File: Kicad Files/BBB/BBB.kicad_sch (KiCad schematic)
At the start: 36 parts, among them J1 PPTC041LFBN-RC, J2 PPTC041LFBN-RC, J3 PPTC041LFBN-RC, J4 PPTC061LFBN-RC, J5 Jumper_NO, J6 PPTC041LFBN-RC, P1 3220-20-0200-00, U1 STM32WBA50KGU6, U2 LM393F-GE2, Y1 ABS07AIG-32.768KHZ-T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

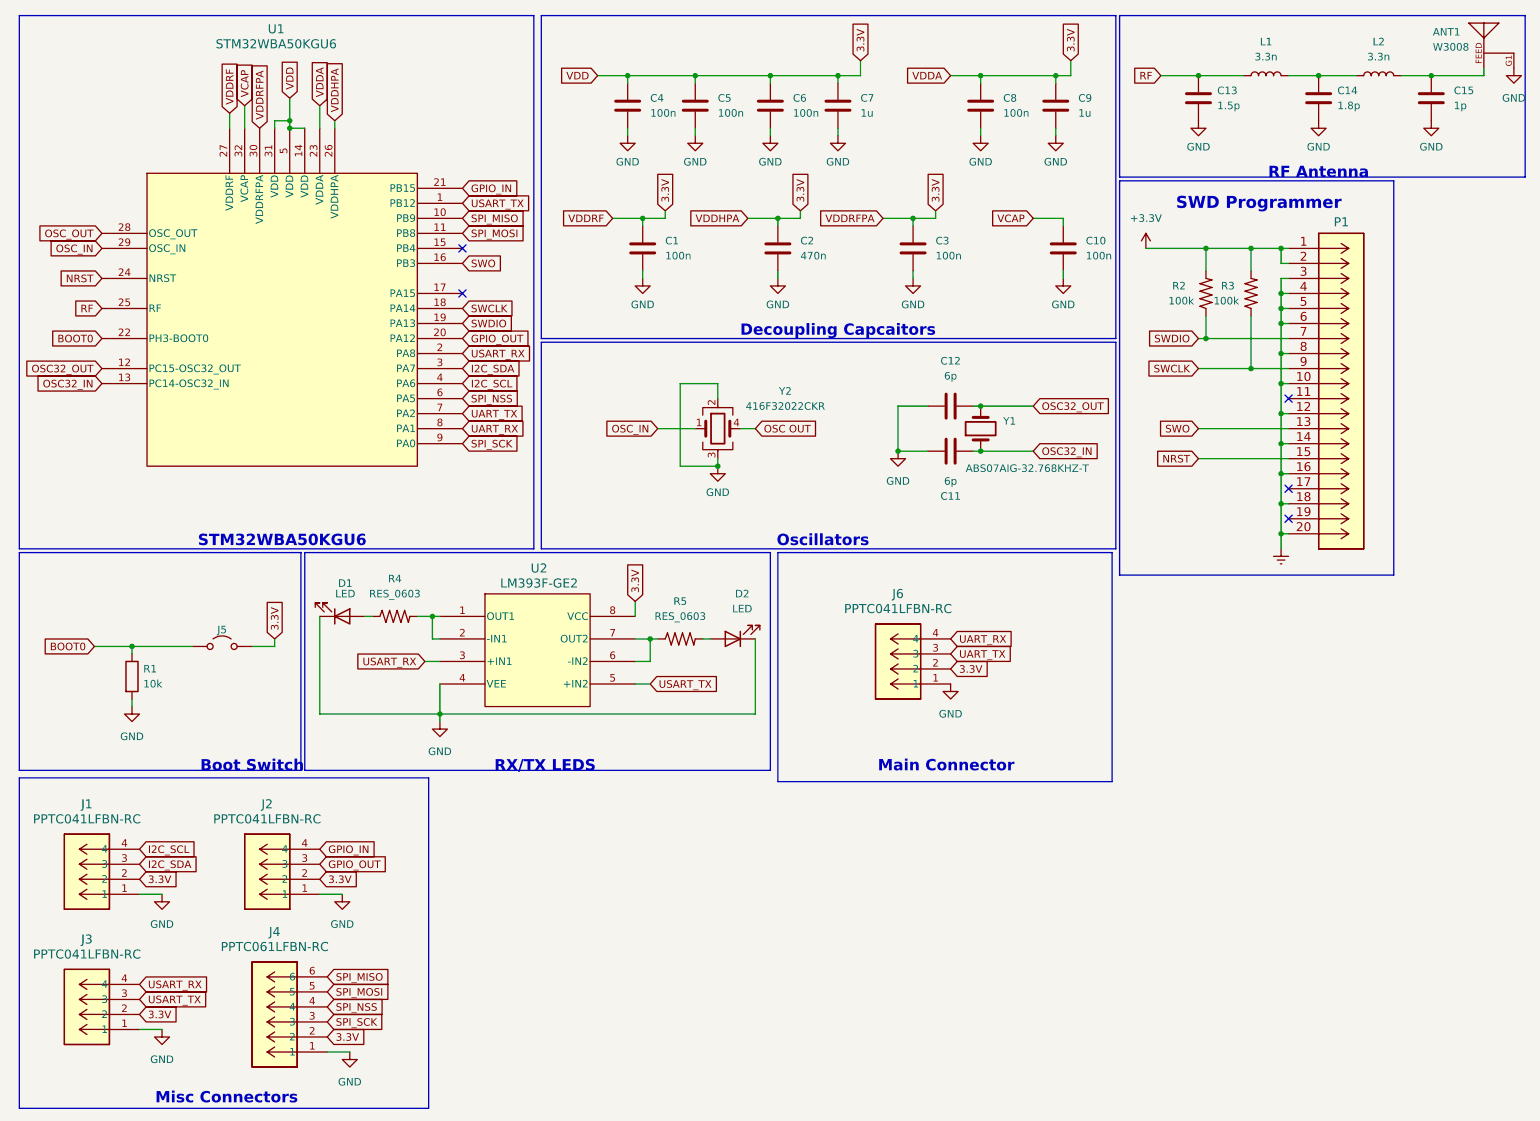
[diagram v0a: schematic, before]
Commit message: BBB Board
Designed basic breakout board for the STMWBA chip
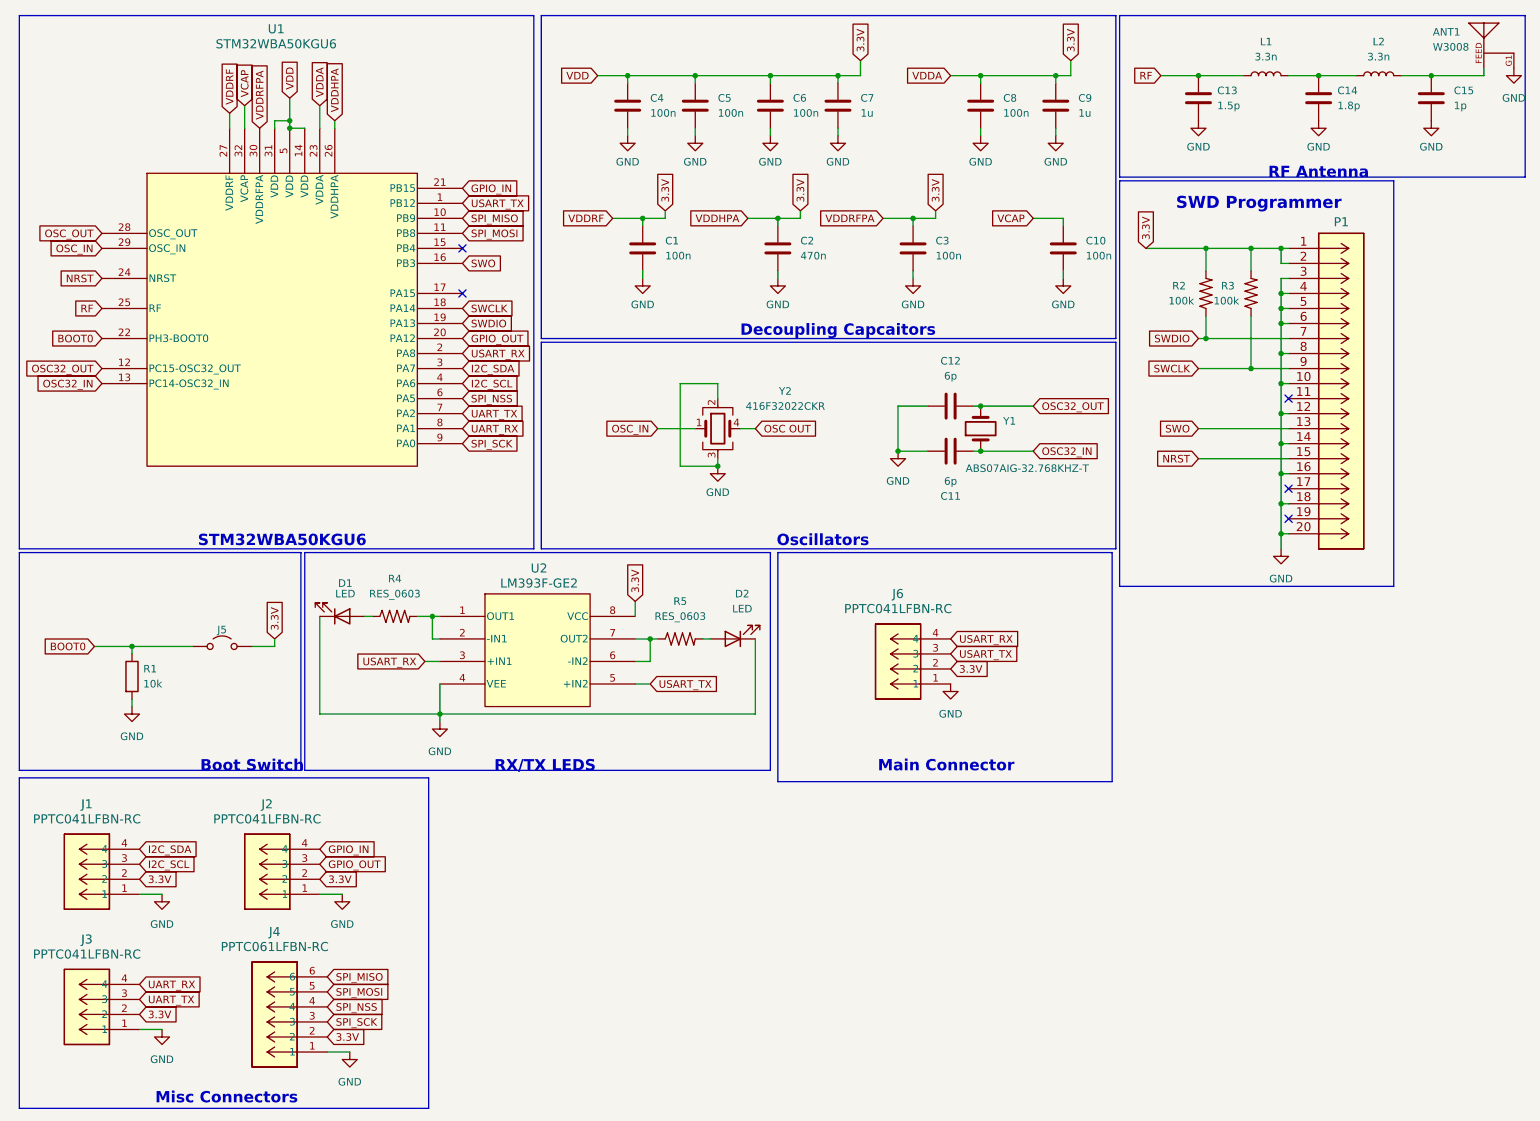
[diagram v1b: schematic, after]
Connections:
- net +3.3V is gone; now on net 3.3V: P1.1, P1.2, R2.2, R3.2
- net Earth is gone; now on net GND: P1.10, P1.12, P1.14, P1.16, P1.18, P1.20, P1.3, P1.4, P1.5, P1.6, P1.8
- net I2C_SCL: now also J1.3; no longer J1.4
- net I2C_SDA: now also J1.4; no longer J1.3
- net UART_RX: now also J3.4; no longer J6.4
- net UART_TX: now also J3.3; no longer J6.3
- net USART_RX: now also J6.4; no longer J3.4
- net USART_TX: now also J6.3; no longer J3.3
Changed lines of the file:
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@@
 	(rectangle
 		(start 198.755 40.64)
-		(end 245.11 107.315)
+		(end 245.11 109.22)
 		(stroke
 			(width 0)
@@
 		)
 	)
+	(global_label "3.3V"
+		(shape input)
+		(at 203.2 52.07 90)
+		(fields_autoplaced yes)
+		(effects
+			(font
+				(size 1.27 1.27)
+			)
+			(justify left)
+		)
+		(property "Intersheetrefs" "${INTERSHEET_REFS}"
+			(at 203.2 44.9724 90)
+			(effects
+				(font
+					(size 1.27 1.27)
+				)
+				(justify left)
+				(hide yes)
+			)
+		)
+	)
 	(global_label "RF"
 		(shape input)
@@
 		)
 	)
-	(global_label "I2C_SCL"
+	(global_label "I2C_SDA"
 		(shape input)
 		(at 33.02 153.67 0)
@@
 		)
 		(property "Intersheetrefs" "${INTERSHEET_REFS}"
-			(at 43.5647 153.67 0)
+			(at 43.6252 153.67 0)
 			(effects
 				(font
@@
 		)
 	)
-	(global_label "I2C_SDA"
+	(global_label "I2C_SCL"
 		(shape input)
 		(at 33.02 156.21 0)
@@
 		)
 		(property "Intersheetrefs" "${INTERSHEET_REFS}"
-			(at 43.6252 156.21 0)
+			(at 43.5647 156.21 0)
 			(effects
 				(font
@@
 		)
 	)
-	(global_label "UART_TX"
+	(global_label "USART_TX"
 		(shape input)
 		(at 170.18 120.65 0)
@@
 		)
 		(property "Intersheetrefs" "${INTERSHEET_REFS}"
-			(at 180.9666 120.65 0)
+			(at 182.1761 120.65 0)
 			(effects
 				(font
@@
 		)
 	)
-	(global_label "USART_TX"
+	(global_label "UART_TX"
 		(shape input)
 		(at 33.02 179.07 0)
@@
 		)
 		(property "Intersheetrefs" "${INTERSHEET_REFS}"
-			(at 45.0161 179.07 0)
+			(at 43.8066 179.07 0)
 			(effects
 				(font
@@
 		)
 	)
-	(global_label "USART_RX"
+	(global_label "UART_RX"
 		(shape input)
 		(at 33.02 176.53 0)
@@
 		)
 		(property "Intersheetrefs" "${INTERSHEET_REFS}"
-			(at 45.3185 176.53 0)
+			(at 44.109 176.53 0)
 			(effects
 				(font
@@
 		)
 	)
-	(global_label "UART_RX"
+	(global_label "USART_RX"
 		(shape input)
 		(at 170.18 118.11 0)
@@
 		)
 		(property "Intersheetrefs" "${INTERSHEET_REFS}"
-			(at 181.269 118.11 0)
+			(at 182.4785 118.11 0)
 			(effects
 				(font
@@
 	)
 	(symbol
+		(lib_id "power:GND")
+		(at 226.06 102.87 0)
+		(unit 1)
+		(exclude_from_sim no)
+		(in_bom yes)
+		(on_board yes)
+		(dnp no)
+		(fields_autoplaced yes)
+		(property "Reference" "#PWR01"
+			(at 226.06 109.22 0)
+			(effects
+				(font
+					(size 1.27 1.27)
+				)
+				(hide yes)
+			)
+		)
+		(property "Value" "GND"
+			(at 226.06 107.95 0)
+			(effects
+				(font
+					(size 1.27 1.27)
+				)
+			)
+		)
+		(property "Footprint" ""
+			(at 226.06 102.87 0)
+			(effects
+				(font
+					(size 1.27 1.27)
+				)
+				(hide yes)
+			)
+		)
+		(property "Datasheet" ""
+			(at 226.06 102.87 0)
+			(effects
+				(font
+					(size 1.27 1.27)
+				)
+				(hide yes)
+			)
+		)
+		(property "Description" "Power symbol creates a global label with name \"GND\" , ground"
+			(at 226.06 102.87 0)
+			(effects
+				(font
+					(size 1.27 1.27)
+				)
+				(hide yes)
+			)
+		)
+		(pin "1"
+		)
+		(instances
+			(project "BBB"
+				(path "/bb418d4c-b3c1-45ea-bc1d-244bd471de35"
+					(reference "#PWR01")
+					(unit 1)
+				)
+			)
+		)
+	)
+	(symbol
 		(lib_name "PPTC041LFBN-RC_1")
 		(lib_id "PPTC061:PPTC041LFBN-RC")
@@
 	)
 	(symbol
-		(lib_id "power:+3.3V")
-		(at 203.2 52.07 0)
-		(unit 1)
-		(exclude_from_sim no)
-		(in_bom yes)
-		(on_board yes)
-		(dnp no)
-		(fields_autoplaced yes)
-		(property "Reference" "#PWR024"
-			(at 203.2 55.88 0)
-			(effects
-				(font
-					(size 1.27 1.27)
-				)
-				(hide yes)
-			)
-		)
-		(property "Value" "+3.3V"
-			(at 203.2 46.99 0)
-			(effects
-				(font
-					(size 1.27 1.27)
-				)
-			)
-		)
-		(property "Footprint" ""
-			(at 203.2 52.07 0)
-			(effects
-				(font
-					(size 1.27 1.27)
-				)
-				(hide yes)
-			)
-		)
-		(property "Datasheet" ""
-			(at 203.2 52.07 0)
-			(effects
-				(font
-					(size 1.27 1.27)
-				)
-				(hide yes)
-			)
-		)
-		(property "Description" "Power symbol creates a global label with name \"+3.3V\""
-			(at 203.2 52.07 0)
-			(effects
-				(font
-					(size 1.27 1.27)
-				)
-				(hide yes)
-			)
-		)
-		(pin "1"
-		)
-		(instances
-			(project ""
-				(path "/bb418d4c-b3c1-45ea-bc1d-244bd471de35"
-					(reference "#PWR024")
-					(unit 1)
-				)
-			)
-		)
-	)
-	(symbol
 		(lib_id "Flight-Computer:RES_0603")
 		(at 124.46 118.11 0)
@@
 					(unit 1)
 				)
-			)
-		)
-	)
-	(symbol
-		(lib_id "Flight-Computer:Earth")
-		(at 226.06 102.87 0)
-		(unit 1)
-		(exclude_from_sim no)
-		(in_bom yes)
-		(on_board yes)
-		(dnp no)
-		(fields_autoplaced yes)
-		(property "Reference" "#PWR018"
-			(at 226.06 109.22 0)
-			(effects
-				(font
-					(size 1.27 1.27)
-				)
-				(hide yes)
-			)
-		)
-		(property "Value" "Earth"
-			(at 226.06 106.68 0)
-			(effects
-				(font
-					(size 1.27 1.27)
-				)
-				(hide yes)
-			)
-		)
-		(property "Footprint" ""
-			(at 226.06 102.87 0)
-			(effects
-				(font
-					(size 1.27 1.27)
-				)
-				(hide yes)
-			)
-		)
-		(property "Datasheet" ""
-			(at 226.06 102.87 0)
-			(effects
-				(font
-					(size 1.27 1.27)
-				)
-				(hide yes)
-			)
-		)
-		(property "Description" ""
-			(at 226.06 102.87 0)
-			(effects
-				(font
-					(size 1.27 1.27)
-				)
-				(hide yes)
-			)
-		)
-		(pin "1"
-		)
-		(instances
-			(project "BBB"
-				(path "/bb418d4c-b3c1-45ea-bc1d-244bd471de35"
-					(reference "#PWR018")
-					(unit 1)
-				)
